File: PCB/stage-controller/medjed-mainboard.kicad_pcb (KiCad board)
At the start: 4 copper layers, 125 x 60 mm, 104 parts, among them J1 Barrel_Jack, J2 ESTOP terminal, J3 Conn_01x04_Pin, SW2 ESTOP switch, U1 P78E-1000, U10 TCAN330, U11 teensy 4.1, U12 MIC5317-3.3, U13 MIC5317-1.8, U17 TMC4361A-LA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

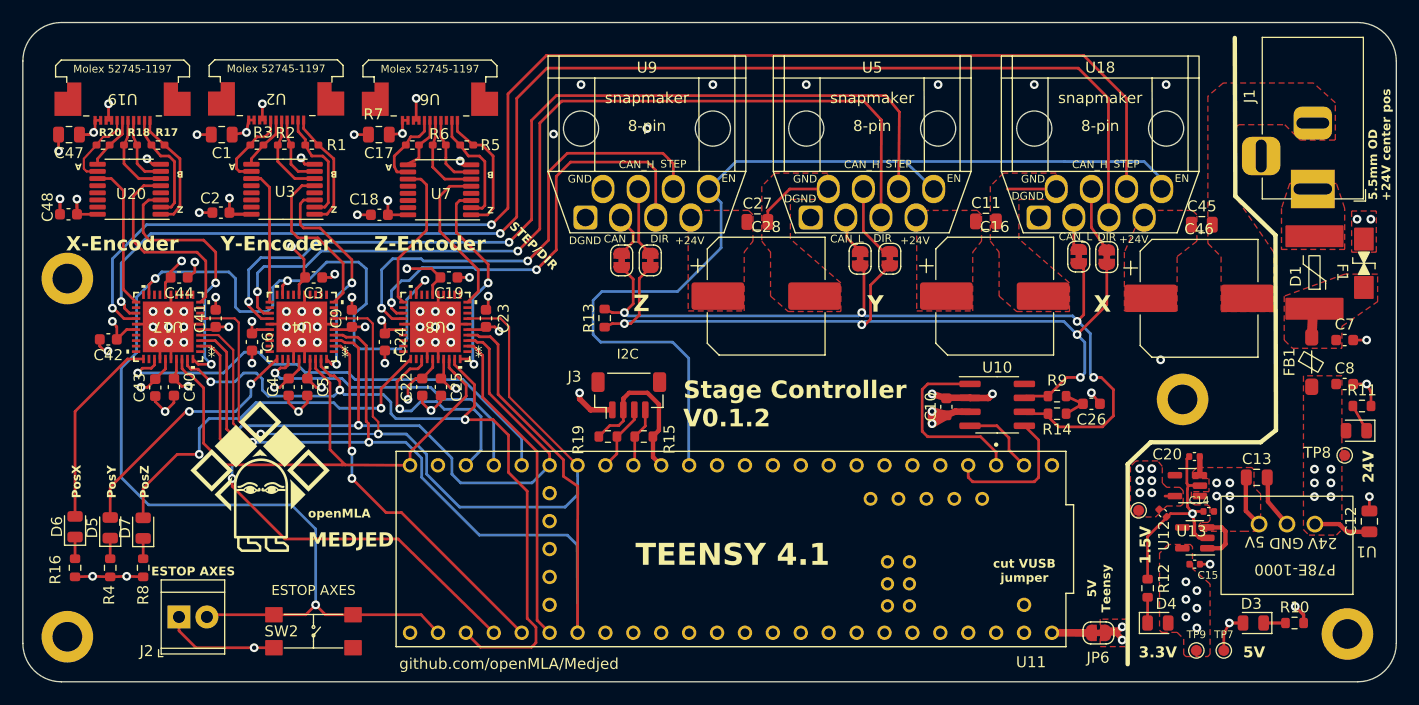
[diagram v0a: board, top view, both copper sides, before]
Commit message: Update PCB files
Pre-removal and submodule reorganisation
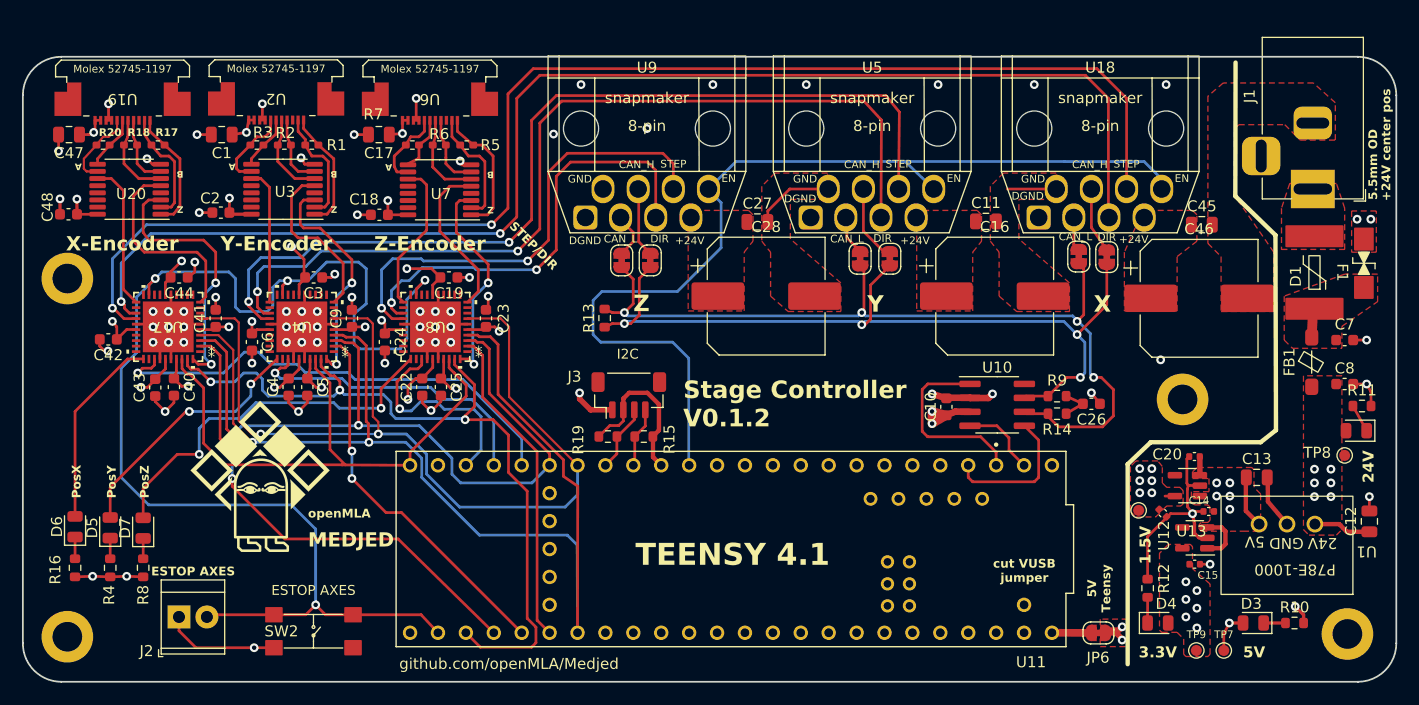
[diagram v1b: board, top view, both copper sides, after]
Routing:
- net /Axis X/STEP: track 123.1 -> 122.1 mm
- net /Axis X/DIR: track 121.0 -> 120.5 mm
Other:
- board size 125 x 60 mm -> 125 x 56.9 mm
